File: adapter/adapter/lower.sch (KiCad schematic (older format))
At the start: 12 parts, among them J1 MALE, J2 FEMALE, J3 STANDOFF, J4 STANDOFF, J5 DTR

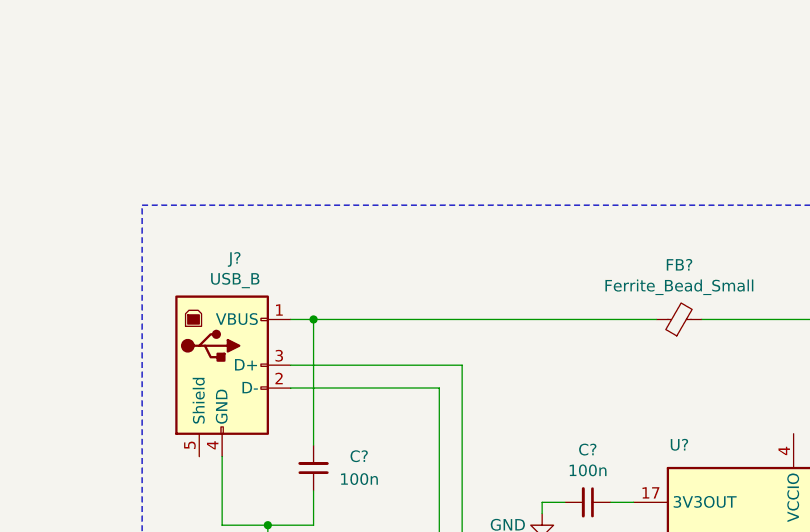
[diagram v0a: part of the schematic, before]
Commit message: Add resettable fuse (don’t connect yet)
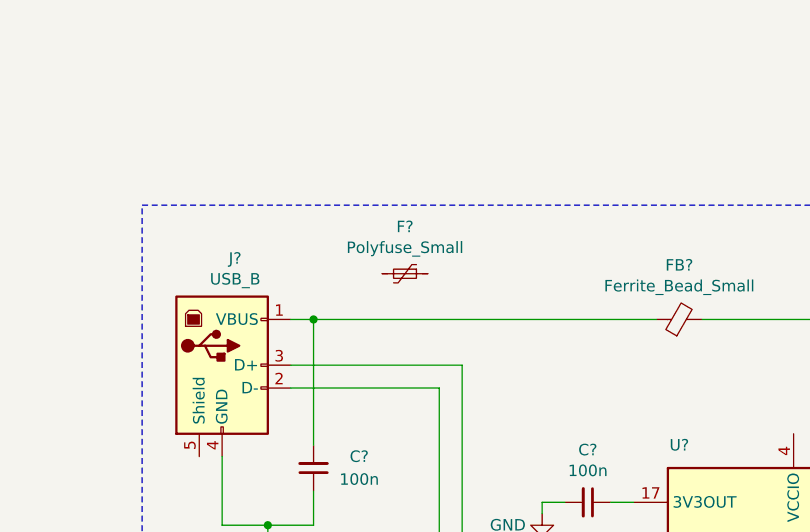
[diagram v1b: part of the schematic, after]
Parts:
- added F?: Polyfuse_Small, symbol Device:Polyfuse_Small
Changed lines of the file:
@@
 NoConn ~ 7050 3900
 NoConn ~ 7050 4100
+$Comp
+L Device:Polyfuse_Small F?
+U 1 1 5FAB1773
+P 6050 2000
+F 0 "F?" V 5845 2000 50  0000 C CNN
+F 1 "Polyfuse_Small" V 5936 2000 50  0000 C CNN
+F 2 "" H 6100 1800 50  0001 L CNN
+F 3 "~" H 6050 2000 50  0001 C CNN
+	1    6050 2000
+	0    1    1    0
+$EndComp
 $EndSCHEMATC
